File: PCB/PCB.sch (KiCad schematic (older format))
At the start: 105 parts, among them J1 Conn_01x01_MountingPin, J2 Conn, J3 Screw_Terminal_01x02, J4 Screw_Terminal_01x02, J5 Screw_Terminal_01x02, J6 Screw_Terminal_01x02, J7 Conn_01x01_MountingPin, Q1 Q_NPN_BCE, Q10 Q_NPN, Q11 Q_PNP_BCE, Q12 Q_NPN, Q13 Q_PNP, Q14 Q_PNP_BCE, Q15 Q_PNP_BCE, Q16 Q-NPN, Q17 Q-NPN, Q18 Q-NPN, Q19 Q-PNP, Q2 Q_PNP_BCE, Q20 Q-NPN, Q21 Q-PNP, Q22 Q-NPN, Q23 Q-PNP, Q24 Q-PNP, Q25 Q-NPN, Q26 Q-NPN, Q27 Q-PNP, Q28 Q-NPN, Q29 Q_PNP, Q3 Q_NPN_BCE, Q4 Q_PNP_BCE, Q5 Q_NPN_BCE, Q6 Q_PNP_BCE, Q7 Q_PNP_BCE, Q8 Q_NPN_BCE, Q9 Q_NPN_BCE

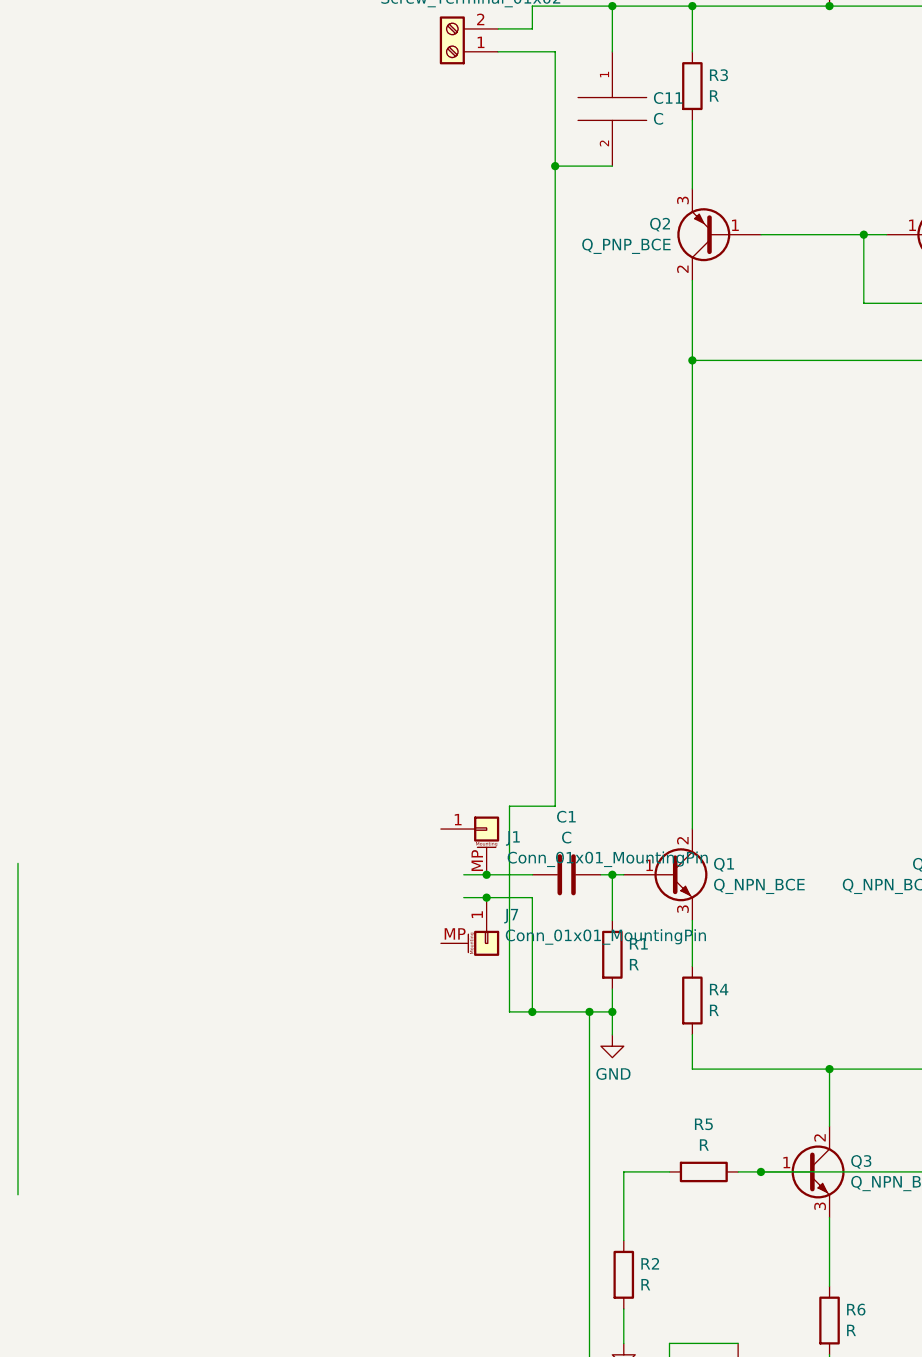
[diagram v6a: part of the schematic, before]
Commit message: Rellenos PROLIJOS, Jack 3.5mm
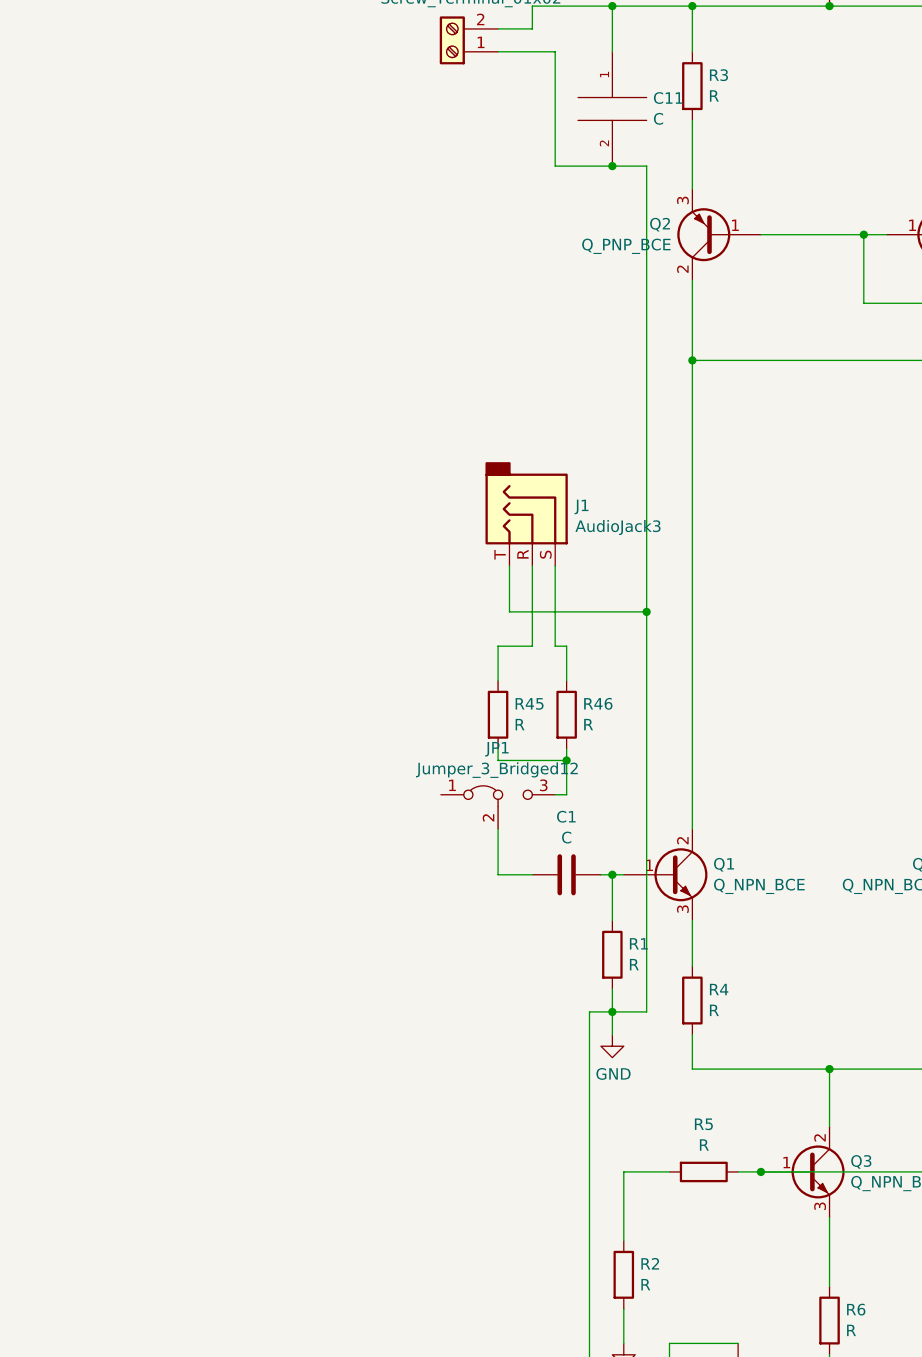
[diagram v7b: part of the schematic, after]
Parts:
- removed J1, J7: Conn_01x01_MountingPin, symbol Connector_Generic_MountingPin:Conn_01x01_MountingPin
- added J1: AudioJack3, Connector:PJ320D_3.5mm_Jack, symbol Connector:AudioJack3
- added JP1: Jumper_3_Bridged12, Connector:Fan_Pin_Header_Straight_1x03, symbol Jumper:Jumper_3_Bridged12
- added R45, R46: R, Resistor_SMD:R_0805_2012Metric_Pad1.15x1.40mm_HandSolder, symbol Device:R
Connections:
- net GND: now also J1.T
- net at C1.1: now also JP1.2 (C)
- new net: J1.S, R46.1
- new net: JP1.3 (B), R45.2, R46.2
- new net: J1.R, R45.1
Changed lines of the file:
@@
 EESchema Schematic File Version 4
 LIBS:PCB-cache
-EELAYER 30 0
+EELAYER 29 0
 EELAYER END
 $Descr A4 11693 8268
@@
 	1350 4550 1300 4550
 Connection ~ 1300 4550
-Wire Wire Line
-	950  4650 950  5150
-Wire Wire Line
-	950  5150 1200 5150
 Connection ~ 1300 5150
 Wire Wire Line
@@
 	1050 950  1050 1450
 Wire Wire Line
-	1050 4250 850  4250
-Wire Wire Line
-	850  4250 850  5150
-Wire Wire Line
-	850  5150 950  5150
-Connection ~ 950  5150
-Connection ~ 1200 5150
-Wire Wire Line
 	1200 5150 1300 5150
 Wire Wire Line
@@
 	10450 5100 10350 5100
 Wire Wire Line
-	-1300 5950 -1300 4500
-Wire Wire Line
 	10350 3650 10650 3650
-Wire Wire Line
-	950  4650 750  4650
-Wire Wire Line
-	950  4550 750  4550
-$Comp
-L Connector_Generic_MountingPin:Conn_01x01_MountingPin J1
-U 1 1 5D48F635
-P 750 4350
-F 0 "J1" H 838 4314 50  0000 L CNN
-F 1 "Conn_01x01_MountingPin" H 838 4223 50  0000 L CNN
-F 2 "" H 750 4350 50  0001 C CNN
-F 3 "~" H 750 4350 50  0001 C CNN
-	1    750  4350
-	1    0    0    -1
-$EndComp
-Connection ~ 750  4550
-Wire Wire Line
-	750  4550 650  4550
-$Comp
-L Connector_Generic_MountingPin:Conn_01x01_MountingPin J7
-U 1 1 5D491977
-P 750 4850
-F 0 "J7" V 626 4930 50  0000 L CNN
-F 1 "Conn_01x01_MountingPin" V 717 4930 50  0000 L CNN
-F 2 "" H 750 4850 50  0001 C CNN
-F 3 "~" H 750 4850 50  0001 C CNN
-	1    750  4850
-	0    1    1    0
-$EndComp
-Connection ~ 750  4650
-Wire Wire Line
-	750  4650 650  4650
 $Comp
 L pspice:C C13
@@
 Wire Wire Line
 	1300 1450 1050 1450
-Connection ~ 1050 1450
-Wire Wire Line
-	1050 1450 1050 4250
 Wire Wire Line
 	1850 7100 1850 7150
@@
 Wire Wire Line
 	10600 2400 10600 3150
+Wire Wire Line
+	1300 5150 1450 5150
+Wire Wire Line
+	1450 5150 1450 3400
+Wire Wire Line
+	1450 1450 1300 1450
+Connection ~ 1300 1450
+$Comp
+L Device:R R46
+U 1 1 5DA42EE5
+P 1100 3850
+F 0 "R46" H 1170 3896 50  0000 L CNN
+F 1 "R" H 1170 3805 50  0000 L CNN
+F 2 "Resistor_SMD:R_0805_2012Metric_Pad1.15x1.40mm_HandSolder" V 1030 3850 50  0001 C CNN
+F 3 "~" H 1100 3850 50  0001 C CNN
+	1    1100 3850
+	1    0    0    -1
+$EndComp
+$Comp
+L Device:R R45
+U 1 1 5DA44CEB
+P 800 3850
+F 0 "R45" H 870 3896 50  0000 L CNN
+F 1 "R" H 870 3805 50  0000 L CNN
+F 2 "Resistor_SMD:R_0805_2012Metric_Pad1.15x1.40mm_HandSolder" V 730 3850 50  0001 C CNN
+F 3 "~" H 800 3850 50  0001 C CNN
+	1    800  3850
+	1    0    0    -1
+$EndComp
+$Comp
+L Jumper:Jumper_3_Bridged12 JP1
+U 1 1 5DA5BC24
+P 800 4200
+F 0 "JP1" H 800 4404 50  0000 C CNN
+F 1 "Jumper_3_Bridged12" H 800 4313 50  0000 C CNN
+F 2 "Connector:Fan_Pin_Header_Straight_1x03" H 800 4200 50  0001 C CNN
+F 3 "~" H 800 4200 50  0001 C CNN
+	1    800  4200
+	1    0    0    -1
+$EndComp
+Wire Wire Line
+	800  4000 800  4050
+Wire Wire Line
+	800  4050 1100 4050
+Wire Wire Line
+	1100 4050 1100 4000
+Wire Wire Line
+	1050 4200 1100 4200
+Wire Wire Line
+	1100 4200 1100 4050
+Connection ~ 1100 4050
+Wire Wire Line
+	800  4350 800  4550
+Wire Wire Line
+	800  4550 950  4550
+$Comp
+L Connector:AudioJack3 J1
+U 1 1 5DAA0416
+P 950 3000
+F 0 "J1" V 886 3188 50  0000 L CNN
+F 1 "AudioJack3" V 977 3188 50  0000 L CNN
+F 2 "Connector:PJ320D_3.5mm_Jack" H 950 3000 50  0001 C CNN
+F 3 "~" H 950 3000 50  0001 C CNN
+	1    950  3000
+	0    1    1    0
+$EndComp
+Wire Wire Line
+	1050 3200 1050 3550
+Wire Wire Line
+	1050 3550 1100 3550
+Wire Wire Line
+	1100 3550 1100 3700
+Wire Wire Line
+	950  3550 800  3550
+Wire Wire Line
+	800  3550 800  3700
+Wire Wire Line
+	950  3200 950  3550
+Wire Wire Line
+	850  3200 850  3400
+Wire Wire Line
+	850  3400 1450 3400
+Connection ~ 1450 3400
+Wire Wire Line
+	1450 3400 1450 1450
 $EndSCHEMATC

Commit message: update
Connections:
- net at J1.R, R45.1: now also JP1.1 (A)
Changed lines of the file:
@@
 Wire Wire Line
 	1450 3400 1450 1450
+Wire Wire Line
+	550  4200 550  3550
+Wire Wire Line
+	550  3550 800  3550
+Connection ~ 800  3550
 $EndSCHEMATC
